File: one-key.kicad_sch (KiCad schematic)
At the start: 3 parts, among them SW1 SW_SPST

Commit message: 
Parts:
- SW1: footprint (none) -> key-switches:SW_MX_HotSwap_THT
- TP1, TP2: footprint (none) -> TestPoint:TestPoint_Pad_1.0x1.0mm
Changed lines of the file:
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@@
 			)
 		)
-		(property "Footprint" ""
+		(property "Footprint" "TestPoint:TestPoint_Pad_1.0x1.0mm"
 			(at 151.13 77.47 0)
 			(effects
@@
 			)
 		)
-		(property "Footprint" ""
+		(property "Footprint" "TestPoint:TestPoint_Pad_1.0x1.0mm"
 			(at 127 77.47 0)
 			(effects
@@
 			)
 		)
-		(property "Footprint" ""
+		(property "Footprint" "key-switches:SW_MX_HotSwap_THT"
 			(at 138.43 82.55 0)
 			(effects

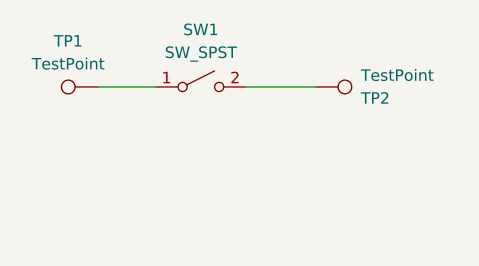
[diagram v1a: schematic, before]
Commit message: 
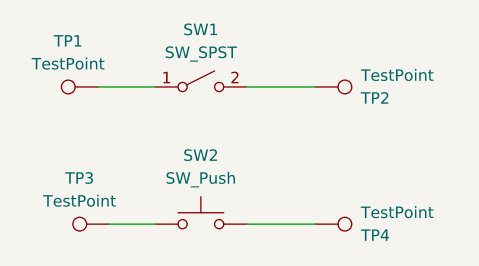
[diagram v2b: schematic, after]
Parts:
- added SW2: SW_Push, key-switches:SW_Kailh_Choc_V1_HotSwap, symbol Switch:SW_Push
- added TP3, TP4: TestPoint, TestPoint:TestPoint_Pad_1.0x1.0mm, symbol Connector:TestPoint
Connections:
- new net: SW2.2, TP4.1
- new net: SW2.1, TP3.1
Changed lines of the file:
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@@
+	(wire
+		(pts
+			(xy 143.51 97.79) (xy 151.13 97.79)
+		)
+		(stroke
+			(width 0)
+			(type default)
+		)
+	)
 	(wire
 		(pts
@@
 	(wire
 		(pts
-			(xy 143.51 82.55) (xy 151.13 82.55)
+			(xy 128.27 97.79) (xy 133.35 97.79)
 		)
 		(stroke
@@
 		)
 	)
+	(wire
+		(pts
+			(xy 143.51 82.55) (xy 151.13 82.55)
+		)
+		(stroke
+			(width 0)
+			(type default)
+		)
+	)
+	(symbol
+		(lib_id "Connector:TestPoint")
+		(at 151.13 97.79 270)
+		(mirror x)
+		(unit 1)
+		(exclude_from_sim no)
+		(in_bom yes)
+		(on_board yes)
+		(dnp no)
+		(property "Reference" "TP4"
+			(at 156.21 99.0601 90)
+			(effects
+				(font
+					(size 1.27 1.27)
+				)
+				(justify left)
+			)
+		)
+		(property "Value" "TestPoint"
+			(at 156.21 96.5201 90)
+			(effects
+				(font
+					(size 1.27 1.27)
+				)
+				(justify left)
+			)
+		)
+		(property "Footprint" "TestPoint:TestPoint_Pad_1.0x1.0mm"
+			(at 151.13 92.71 0)
+			(effects
+				(font
+					(size 1.27 1.27)
+				)
+				(hide yes)
+			)
+		)
+		(property "Datasheet" "~"
+			(at 151.13 92.71 0)
+			(effects
+				(font
+					(size 1.27 1.27)
+				)
+				(hide yes)
+			)
+		)
+		(property "Description" "test point"
+			(at 151.13 97.79 0)
+			(effects
+				(font
+					(size 1.27 1.27)
+				)
+				(hide yes)
+			)
+		)
+		(pin "1"
+		)
+		(instances
+			(project "one-key"
+				(path "/3cb37580-4502-420b-ab15-4dcda6c99b22"
+					(reference "TP4")
+					(unit 1)
+				)
+			)
+		)
+	)
 	(symbol
 		(lib_id "Connector:TestPoint")
@@
 	)
 	(symbol
+		(lib_id "Switch:SW_Push")
+		(at 138.43 97.79 0)
+		(unit 1)
+		(exclude_from_sim no)
+		(in_bom yes)
+		(on_board yes)
+		(dnp no)
+		(fields_autoplaced yes)
+		(property "Reference" "SW2"
+			(at 138.43 90.17 0)
+			(effects
+				(font
+					(size 1.27 1.27)
+				)
+			)
+		)
+		(property "Value" "SW_Push"
+			(at 138.43 92.71 0)
+			(effects
+				(font
+					(size 1.27 1.27)
+				)
+			)
+		)
+		(property "Footprint" "key-switches:SW_Kailh_Choc_V1_HotSwap"
+			(at 138.43 92.71 0)
+			(effects
+				(font
+					(size 1.27 1.27)
+				)
+				(hide yes)
+			)
+		)
+		(property "Datasheet" "~"
+			(at 138.43 92.71 0)
+			(effects
+				(font
+					(size 1.27 1.27)
+				)
+				(hide yes)
+			)
+		)
+		(property "Description" "Push button switch, generic, two pins"
+			(at 138.43 97.79 0)
+			(effects
+				(font
+					(size 1.27 1.27)
+				)
+				(hide yes)
+			)
+		)
+		(pin "1"
+		)
+		(pin "2"
+		)
+		(instances
+			(project ""
+				(path "/3cb37580-4502-420b-ab15-4dcda6c99b22"
+					(reference "SW2")
+					(unit 1)
+				)
+			)
+		)
+	)
+	(symbol
 		(lib_id "Connector:TestPoint")
 		(at 127 82.55 90)
@@
 					(unit 1)
 				)
+			)
+		)
+	)
+	(symbol
+		(lib_id "Connector:TestPoint")
+		(at 128.27 97.79 90)
+		(unit 1)
+		(exclude_from_sim no)
+		(in_bom yes)
+		(on_board yes)
+		(dnp no)
+		(fields_autoplaced yes)
+		(property "Reference" "TP3"
+			(at 124.968 92.71 90)
+			(effects
+				(font
+					(size 1.27 1.27)
+				)
+			)
+		)
+		(property "Value" "TestPoint"
+			(at 124.968 95.25 90)
+			(effects
+				(font
+					(size 1.27 1.27)
+				)
+			)
+		)
+		(property "Footprint" "TestPoint:TestPoint_Pad_1.0x1.0mm"
+			(at 128.27 92.71 0)
+			(effects
+				(font
+					(size 1.27 1.27)
+				)
+				(hide yes)
+			)
+		)
+		(property "Datasheet" "~"
+			(at 128.27 92.71 0)
+			(effects
+				(font
+					(size 1.27 1.27)
+				)
+				(hide yes)
+			)
+		)
+		(property "Description" "test point"
+			(at 128.27 97.79 0)
+			(effects
+				(font
+					(size 1.27 1.27)
+				)
+				(hide yes)
+			)
+		)
+		(pin "1"
+		)
+		(instances
+			(project "one-key"
+				(path "/3cb37580-4502-420b-ab15-4dcda6c99b22"
+					(reference "TP3")
+					(unit 1)
+				)
